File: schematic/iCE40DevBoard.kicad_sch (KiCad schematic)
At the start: 0 parts

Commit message: Setup schematic
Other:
- added sheet FPGA (FPGA.kicad_sch)
- added sheet Headers (Headers.kicad_sch)
- added sheet Power Supply (PowerSupply.kicad_sch)
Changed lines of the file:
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@@
     (rev "v1")
+  )
+  (sheet (at 139.7 76.2) (size 25.4 12.7)
+    (stroke (width 0.1524) (type solid))
+    (fill (color 0 0 0 0.0000))
+    (property "Sheetname" "Headers" (at 139.7 90.17 0)
+      (effects (font (size 1.27 1.27)) (justify left top))
+    )
+    (property "Sheetfile" "Headers.kicad_sch" (at 139.7 89.4846 0)
+      (effects (font (size 1.27 1.27)) (justify left top) hide)
+    )
+    (instances
+      (project "iCE40DevBoard"
+        (path "/2f10ad52-4a2c-425a-8339-df6126e31315" (page "5"))
+      )
+    )
+  )
+  (sheet (at 76.2 50.8) (size 25.4 12.7) (fields_autoplaced)
+    (stroke (width 0.1524) (type solid))
+    (fill (color 0 0 0 0.0000))
+    (property "Sheetname" "Power Supply" (at 76.2 50.0884 0)
+      (effects (font (size 1.27 1.27)) (justify left bottom))
+    )
+    (property "Sheetfile" "PowerSupply.kicad_sch" (at 76.2 64.0846 0)
+      (effects (font (size 1.27 1.27)) (justify left top) hide)
+    )
+    (instances
+      (project "iCE40DevBoard"
+        (path "/2f10ad52-4a2c-425a-8339-df6126e31315" (page "2"))
+      )
+    )
+  )
+  (sheet (at 139.7 50.8) (size 25.4 12.7) (fields_autoplaced)
+    (stroke (width 0.1524) (type solid))
+    (fill (color 0 0 0 0.0000))
+    (property "Sheetname" "FPGA" (at 139.7 50.0884 0)
+      (effects (font (size 1.27 1.27)) (justify left bottom))
+    )
+    (property "Sheetfile" "FPGA.kicad_sch" (at 139.7 64.0846 0)
+      (effects (font (size 1.27 1.27)) (justify left top) hide)
+    )
+    (instances
+      (project "iCE40DevBoard"
+        (path "/2f10ad52-4a2c-425a-8339-df6126e31315" (page "3"))
+      )
+    )
   )
   (sheet_instances

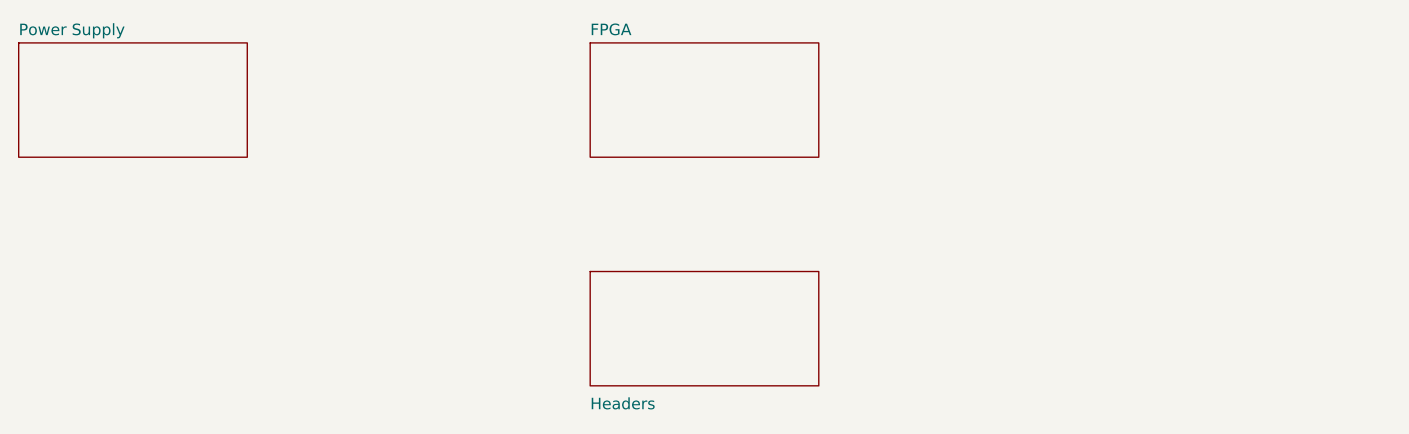
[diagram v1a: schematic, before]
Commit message: Connect FPGA to headers
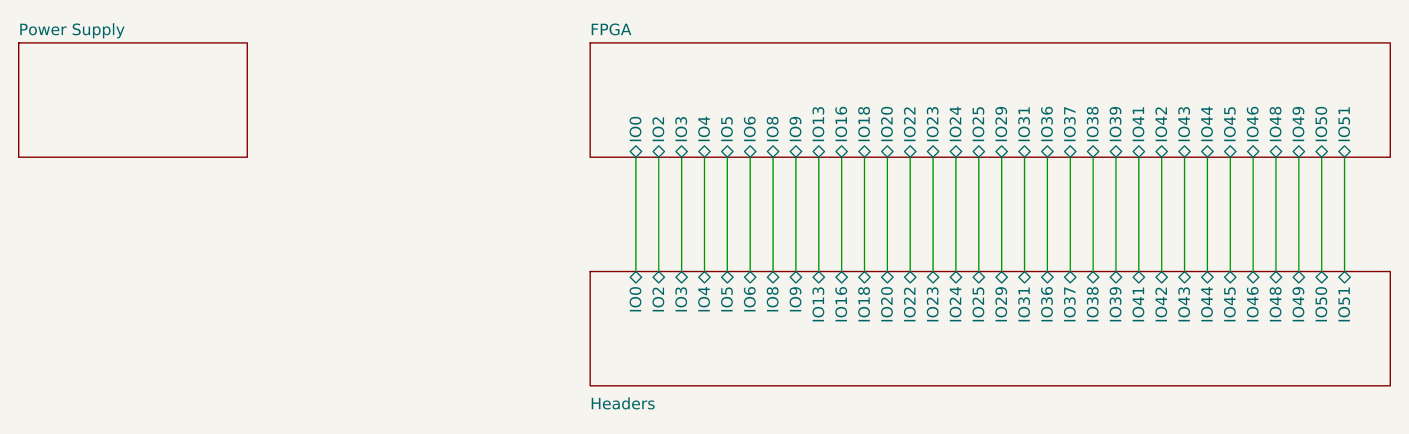
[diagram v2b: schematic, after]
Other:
- sheet FPGA ports: added IO0, IO13, IO16, IO18, IO2, IO20, IO22, IO23, IO24, IO25, IO29, IO3, IO31, IO36, IO37, IO38, IO39, IO4, IO41, IO42, IO43, IO44, IO45, IO46, IO48, IO49, IO5, IO50, IO51, IO6, IO8, IO9; removed none
- sheet Headers ports: added IO0, IO13, IO16, IO18, IO2, IO20, IO22, IO23, IO24, IO25, IO29, IO3, IO31, IO36, IO37, IO38, IO39, IO4, IO41, IO42, IO43, IO44, IO45, IO46, IO48, IO49, IO5, IO50, IO51, IO6, IO8, IO9; removed none
